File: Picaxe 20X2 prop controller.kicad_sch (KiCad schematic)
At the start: 58 parts, among them J1 FC68131, J10 Conn_01x05_Male (- power bus), J11 Conn_01x08_Male - pin I/O, J12 MP3 player, J13 servo 2, J14 servo 3, J15 servo 4, J16 servo 5, J17 Ext servo power, J18 Servo power select, J19 C.0, J2 Conn_01x08_Male - pin I/O, J20 C.5, J21 C.1, J22 C.6, J23 C.2, J24 C.7, J25 C.3, J26 C.4, J27 B.6 TX, J28 OSTTC080162, J29 B.7 RX, J3 servo 1, J4 servo 6, J5 B.7 RX, J6 OSTTC080162, J7 OSTTC020162, J8 PJ-202AH, J9 Conn_01x05_Male (+ power bus), U1 Picaxe 20X2, U3 L7805CV, U4 ULN2803A

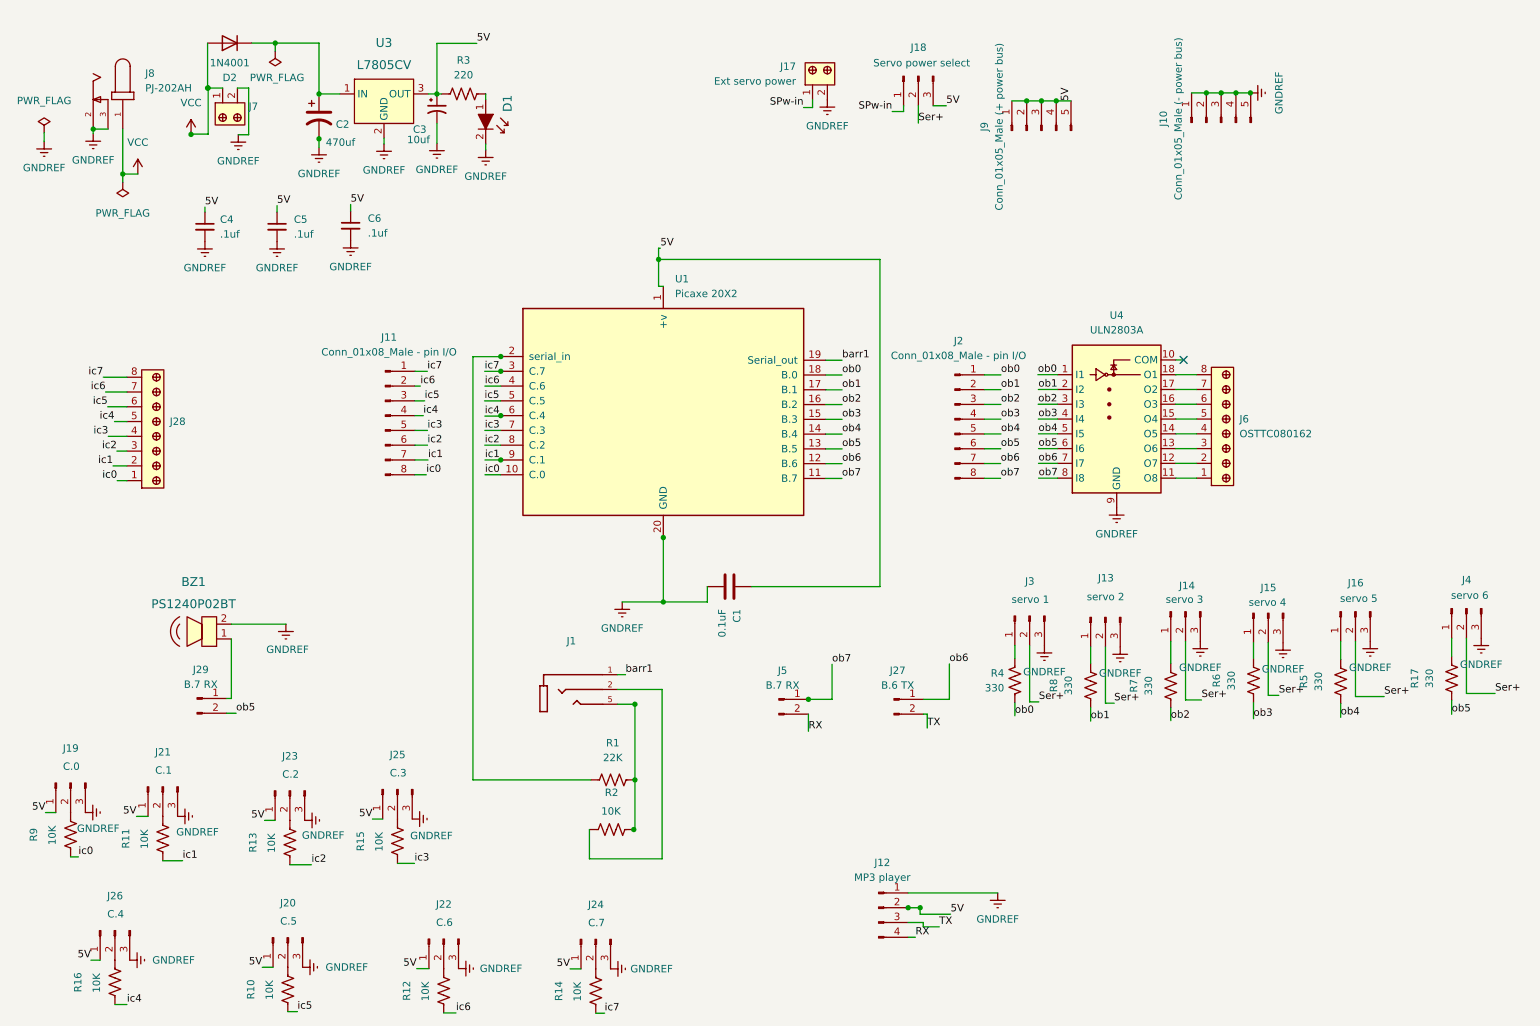
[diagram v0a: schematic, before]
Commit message: Move 20X2 to Git
Will branch to see about moving the I2C connector
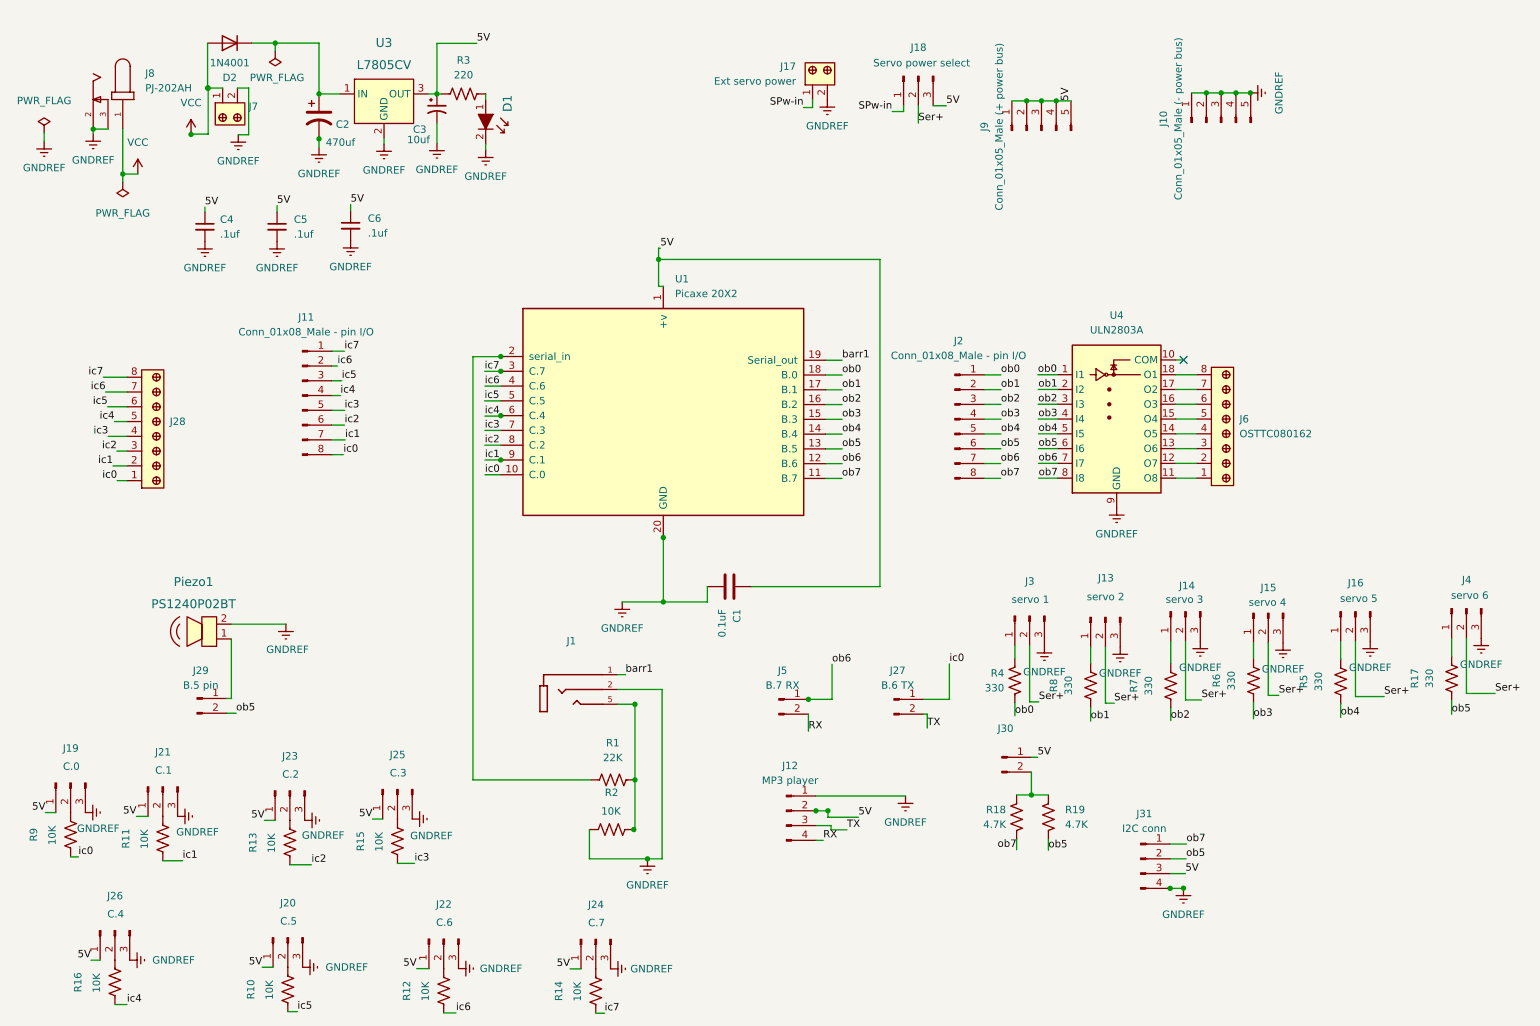
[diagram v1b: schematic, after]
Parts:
- added J30: B.6, Connector_PinHeader_2.54mm:PinHeader_1x02_P2.54mm_Vertical, symbol Connector:Conn_01x02_Male
- added J31: I2C conn, Connector_PinHeader_2.54mm:PinHeader_1x04_P2.54mm_Vertical, symbol Connector:Conn_01x04_Male
- added R18, R19: 4.7K, Resistor_THT:R_Axial_DIN0207_L6.3mm_D2.5mm_P10.16mm_Horizontal, symbol Device:R_US
- J29: value B.7 RX -> B.5 pin
- renumbered BZ1 to Piezo1
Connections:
- net 5V: now also J30.1 (Pin_1), J31.3 (Pin_3)
- net GNDREF: now also J1.2, R2.2, J31.4 (Pin_4)
- net ic0: now also J27.1 (Pin_1)
- net ob5: now also J31.2 (Pin_2), R19.2
- net ob6: now also J5.1 (Pin_1); no longer J27.1 (Pin_1)
- net ob7: now also J31.1 (Pin_1), R18.1; no longer J5.1 (Pin_1)
- new net: J30.2 (Pin_2), R18.2, R19.1
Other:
- moved on the sheet: J11, J12

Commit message: Moved I2C connector and started to add a battery select
Created a branch to move the I2C connector
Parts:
- added J32: B.6, Connector_PinHeader_2.54mm:PinHeader_1x02_P2.54mm_Vertical, symbol Connector:Conn_01x02_Male
- added J?: Batt / Reg select, Connector_PinHeader_2.54mm:PinHeader_1x03_P2.54mm_Vertical, symbol Connector:Conn_01x03_Male
- added J?: Batt Connector, Connector_PinHeader_2.54mm:PinHeader_1x02_P2.54mm_Vertical, symbol Connector:Conn_01x02_Male
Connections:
- net 5V: now also R18.2, R19.1; no longer J30.1 (Pin_1)
- net ob5: now also J32.1 (Pin_1); no longer J31.2 (Pin_2), R19.2
- net ob7: now also J30.1 (Pin_1); no longer J31.1 (Pin_1), R18.1
- new net I2CP1: J30.2 (Pin_2), J31.1 (Pin_1), R18.1
- new net I2CP2: J31.2 (Pin_2), J32.2 (Pin_2), R19.2
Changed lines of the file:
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@@
   (junction (at 216.535 22.6314) (diameter 0) (color 0 0 0 0)
   )
-  (junction (at 186.4614 143.3068) (diameter 0) (color 0 0 0 0)
-  )
   (junction (at 95.25 78.105) (diameter 0) (color 0 0 0 0)
   )
@@
   (junction (at 221.615 22.6314) (diameter 0) (color 0 0 0 0)
   )
+  (junction (at 183.9214 142.875) (diameter 0) (color 0 0 0 0)
+  )
   (junction (at 44.958 21.7932) (diameter 0) (color 0 0 0 0)
   )
@@
   )
   (junction (at 148.1328 126.873) (diameter 0) (color 0 0 0 0)
+  )
+  (junction (at 186.4614 139.3698) (diameter 0) (color 0 0 0 0)
   )
   (junction (at 123.19 110.1344) (diameter 0) (color 0 0 0 0)
@@
     (stroke (width 0) (type default) (color 0 0 0 0))
   )
+  (wire (pts (xy 183.9214 142.875) (xy 183.9214 143.3068))
+    (stroke (width 0) (type default) (color 0 0 0 0))
+  )
   (wire (pts (xy 24.8158 171.704) (xy 26.3906 171.704))
     (stroke (width 0) (type default) (color 0 0 0 0))
@@
     (stroke (width 0) (type default) (color 0 0 0 0))
   )
+  (wire (pts (xy 182.245 142.875) (xy 183.9214 142.875))
+    (stroke (width 0) (type default) (color 0 0 0 0))
+  )
   (wire (pts (xy 95.25 70.485) (xy 95.2754 70.485))
     (stroke (width 0) (type default) (color 0 0 0 0))
@@
     (stroke (width 0) (type default) (color 0 0 0 0))
   )
-  (wire (pts (xy 183.9214 143.3068) (xy 186.4614 143.3068))
-    (stroke (width 0) (type default) (color 0 0 0 0))
-  )
   (wire (pts (xy 187.579 71.0692) (xy 190.9572 71.0692))
     (stroke (width 0) (type default) (color 0 0 0 0))
@@
     (stroke (width 0) (type default) (color 0 0 0 0))
   )
-  (wire (pts (xy 186.4614 139.3698) (xy 186.4614 143.3068))
-    (stroke (width 0) (type default) (color 0 0 0 0))
-  )
   (wire (pts (xy 92.5068 73.025) (xy 95.25 73.025))
     (stroke (width 0) (type default) (color 0 0 0 0))
@@
     (stroke (width 0) (type default) (color 0 0 0 0))
   )
+  (wire (pts (xy 186.436 139.3698) (xy 186.4614 139.3698))
+    (stroke (width 0) (type default) (color 0 0 0 0))
+  )
   (wire (pts (xy 261.239 125.857) (xy 266.1666 125.857))
     (stroke (width 0) (type default) (color 0 0 0 0))
@@
     (stroke (width 0) (type default) (color 0 0 0 0))
   )
+  (wire (pts (xy 202.184 136.8552) (xy 203.4032 136.8552))
+    (stroke (width 0) (type default) (color 0 0 0 0))
+  )
   (wire (pts (xy 151.13 81.28) (xy 153.924 81.28))
     (stroke (width 0) (type default) (color 0 0 0 0))
@@
     (stroke (width 0) (type default) (color 0 0 0 0))
   )
+  (wire (pts (xy 186.4614 139.3698) (xy 187.7568 139.3698))
+    (stroke (width 0) (type default) (color 0 0 0 0))
+  )
   (wire (pts (xy 164.4904 25.8318) (xy 162.5346 25.8318))
     (stroke (width 0) (type default) (color 0 0 0 0))
@@
     (stroke (width 0) (type default) (color 0 0 0 0))
   )
+  (wire (pts (xy 202.184 139.3952) (xy 203.7842 139.3952))
+    (stroke (width 0) (type default) (color 0 0 0 0))
+  )
   (wire (pts (xy 211.2772 88.8492) (xy 214.8586 88.8492))
     (stroke (width 0) (type default) (color 0 0 0 0))
@@
     (stroke (width 0) (type default) (color 0 0 0 0))
   )
+  (wire (pts (xy 189.3824 142.875) (xy 183.9214 142.875))
+    (stroke (width 0) (type default) (color 0 0 0 0))
+  )
   (wire (pts (xy 187.706 88.8492) (xy 190.9572 88.8492))
     (stroke (width 0) (type default) (color 0 0 0 0))
@@
     (stroke (width 0) (type default) (color 0 0 0 0))
   )
-  (wire (pts (xy 186.4614 143.3068) (xy 189.3824 143.3068))
-    (stroke (width 0) (type default) (color 0 0 0 0))
-  )
   (wire (pts (xy 178.3842 78.7146) (xy 181.229 78.7146))
     (stroke (width 0) (type default) (color 0 0 0 0))
@@
     (stroke (width 0) (type default) (color 0 0 0 0))
   )
+  (wire (pts (xy 189.3824 143.3068) (xy 189.3824 142.875))
+    (stroke (width 0) (type default) (color 0 0 0 0))
+  )
   (wire (pts (xy 122.3772 51.2572) (xy 122.3772 49.3268))
     (stroke (width 0) (type default) (color 0 0 0 0))
@@
     (effects (font (size 1.27 1.27)) (justify left bottom))
   )
+  (label "I2CP1" (at 183.9214 152.7302 180)
+    (effects (font (size 1.27 1.27)) (justify right bottom))
+  )
   (label "5V" (at 122.682 49.3268 0)
+    (effects (font (size 1.27 1.27)) (justify left bottom))
+  )
+  (label "I2CP2" (at 203.7842 139.3952 0)
     (effects (font (size 1.27 1.27)) (justify left bottom))
   )
@@
     (effects (font (size 1.27 1.27)) (justify left bottom))
   )
+  (label "I2CP1" (at 187.7568 139.3698 0)
+    (effects (font (size 1.27 1.27)) (justify left bottom))
+  )
   (label "ic1" (at 68.5038 82.2706 0)
     (effects (font (size 1.27 1.27)) (justify left bottom))
@@
     (effects (font (size 1.27 1.27)) (justify left bottom))
   )
+  (label "BR_Sel" (at 30.607 50.419 0)
+    (effects (font (size 1.27 1.27)) (justify left bottom))
+  )
   (label "ob5" (at 187.6806 83.7692 0)
     (effects (font (size 1.27 1.27)) (justify left bottom))
@@
   )
   (label "barr1" (at 153.924 68.58 0)
-    (effects (font (size 1.27 1.27)) (justify left bottom))
-  )
-  (label "ob7" (at 213.106 151.7396 0)
     (effects (font (size 1.27 1.27)) (justify left bottom))
   )
@@
     (effects (font (size 1.27 1.27)) (justify left bottom))
   )
-  (label "ob5" (at 213.0552 154.2796 0)
-    (effects (font (size 1.27 1.27)) (justify left bottom))
-  )
   (label "Ser+" (at 187.7314 127.3048 0)
     (effects (font (size 1.27 1.27)) (justify left bottom))
@@
     (effects (font (size 1.27 1.27)) (justify left bottom))
   )
+  (label "I2CP1" (at 213.106 151.7396 0)
+    (effects (font (size 1.27 1.27)) (justify left bottom))
+  )
   (label "ic4" (at 92.5068 78.1812 0)
     (effects (font (size 1.27 1.27)) (justify left bottom))
@@
     (effects (font (size 1.27 1.27)) (justify left bottom))
   )
-  (label "ob7" (at 183.9214 152.7302 180)
-    (effects (font (size 1.27 1.27)) (justify right bottom))
+  (label "ob7" (at 187.5282 136.8298 0)
+    (effects (font (size 1.27 1.27)) (justify left bottom))
   )
   (label "ob7" (at 181.1782 88.8746 0)
@@
     (effects (font (size 1.27 1.27)) (justify left bottom))
   )
-  (label "5V" (at 187.5282 136.8298 0)
-    (effects (font (size 1.27 1.27)) (justify left bottom))
+  (label "5V" (at 182.245 142.875 180)
+    (effects (font (size 1.27 1.27)) (justify right bottom))
   )
   (label "5V" (at 54.6608 147.6756 180)
@@
     (effects (font (size 1.27 1.27)) (justify right bottom))
   )
-  (label "ob5" (at 189.3824 152.8064 0)
+  (label "ob5" (at 203.4032 136.8552 0)
     (effects (font (size 1.27 1.27)) (justify left bottom))
   )
@@
     (effects (font (size 1.27 1.27)) (justify right bottom))
   )
+  (label "I2CP2" (at 213.0552 154.2796 0)
+    (effects (font (size 1.27 1.27)) (justify left bottom))
+  )
   (label "TX" (at 154.7622 149.3012 0)
     (effects (font (size 1.27 1.27)) (justify left bottom))
@@
   )
   (label "ob3" (at 181.229 78.7146 0)
+    (effects (font (size 1.27 1.27)) (justify left bottom))
+  )
+  (label "I2CP2" (at 189.3824 152.8064 0)
     (effects (font (size 1.27 1.27)) (justify left bottom))
   )
@@
     )
     (pin "1")
+  )
+  (symbol (lib_id "Connector:Conn_01x02_Male") (at 197.104 136.8552 0) (unit 1)
+    (in_bom yes) (on_board yes) (fields_autoplaced)
+    (property "Reference" "J32" (id 0) (at 197.739 131.9022 0))
+    (property "Value" "B.6" (id 1) (at 197.739 134.4422 0)
+      (effects (font (size 1.27 1.27)) hide)
+    )
+    (property "Footprint" "Connector_PinHeader_2.54mm:PinHeader_1x02_P2.54mm_Vertical" (id 2) (at 197.104 136.8552 0)
+      (effects (font (size 1.27 1.27)) hide)
+    )
+    (property "Datasheet" "~" (id 3) (at 197.104 136.8552 0)
+      (effects (font (size 1.27 1.27)) hide)
+    )
+    (pin "1")
+    (pin "2")
   )
   (symbol (lib_id "Picaxe_Joe:LTL2R3KEK") (at 92.6592 28.8544 270) (unit 1)
@@
     (pin "1")
   )
+  (symbol (lib_id "Connector:Conn_01x03_Male") (at 27.3304 62.0522 270) (mirror x) (unit 1)
+    (in_bom yes) (on_board yes)
+    (property "Reference" "J?" (id 0) (at 27.2923 66.9925 90))
+    (property "Value" "Batt / Reg select" (id 1) (at 26.7589 64.3255 90))
+    (property "Footprint" "Connector_PinHeader_2.54mm:PinHeader_1x03_P2.54mm_Vertical" (id 2) (at 27.3304 62.0522 0)
+      (effects (font (size 1.27 1.27)) hide)
+    )
+    (property "Datasheet" "~" (id 3) (at 27.3304 62.0522 0)
+      (effects (font (size 1.27 1.27)) hide)
+    )
+    (pin "1")
+    (pin "2")
+    (pin "3")
+  )
   (symbol (lib_id "Connector:Conn_01x04_Male") (at 144.3482 146.0246 0) (unit 1)
     (in_bom yes) (on_board yes) (fields_autoplaced)
@@
     (pin "1")
   )
+  (symbol (lib_id "Connector:Conn_01x02_Male") (at 20.066 50.2158 0) (unit 1)
+    (in_bom yes) (on_board yes) (fields_autoplaced)
+    (property "Reference" "J?" (id 0) (at 20.701 45.2628 0))
+    (property "Value" "Batt Connector" (id 1) (at 20.701 47.8028 0))
+    (property "Footprint" "Connector_PinHeader_2.54mm:PinHeader_1x02_P2.54mm_Vertical" (id 2) (at 20.066 50.2158 0)
+      (effects (font (size 1.27 1.27)) hide)
+    )
+    (property "Datasheet" "~" (id 3) (at 20.066 50.2158 0)
+      (effects (font (size 1.27 1.27)) hide)
+    )
+    (pin "1")
+    (pin "2")
+  )
   (symbol (lib_id "Connector:Conn_01x03_Male") (at 199.1868 112.776 90) (mirror x) (unit 1)
     (in_bom yes) (on_board yes)
@@
       (reference "J31") (unit 1) (value "I2C conn") (footprint "Connector_PinHeader_2.54mm:PinHeader_1x04_P2.54mm_Vertical")
     )
+    (path "/0bafae2e-441b-4483-84b4-f9087ac28dea"
+      (reference "J32") (unit 1) (value "B.6") (footprint "Connector_PinHeader_2.54mm:PinHeader_1x02_P2.54mm_Vertical")
+    )
+    (path "/571822e8-0e38-4fc2-9bfc-81299bd0b279"
+      (reference "J?") (unit 1) (value "Batt / Reg select") (footprint "Connector_PinHeader_2.54mm:PinHeader_1x03_P2.54mm_Vertical")
+    )
+    (path "/8b60c28b-2164-4b2e-bb66-23cd9efd8df7"
+      (reference "J?") (unit 1) (value "Batt Connector") (footprint "Connector_PinHeader_2.54mm:PinHeader_1x02_P2.54mm_Vertical")
+    )
     (path "/cd32adbb-b86c-4eee-aa17-84272d12d149"

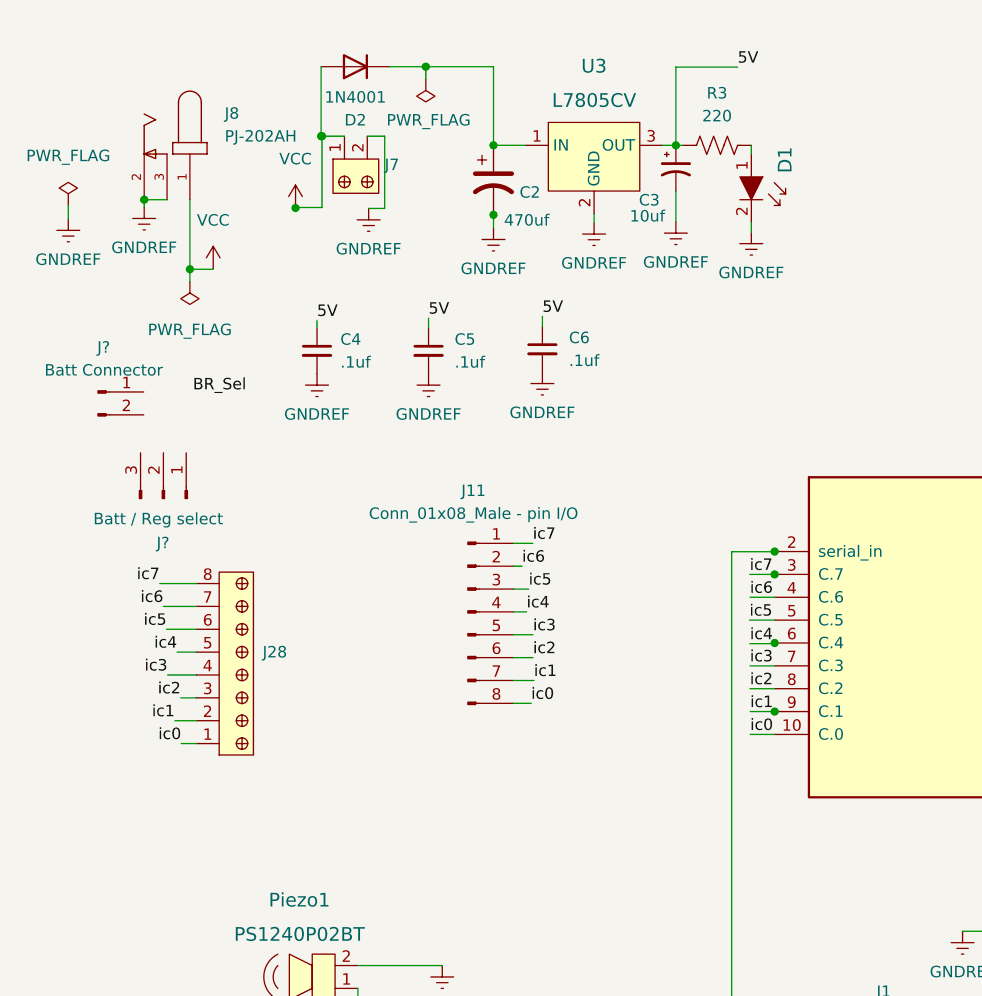
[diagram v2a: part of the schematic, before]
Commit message: Moved I2c connector and added battery select option
Added a battery connector and a select jumper to switch between the onboard regulator and the battery input connector. I also moved the I2C connector and added jumpers to disconnect the pins if needed.
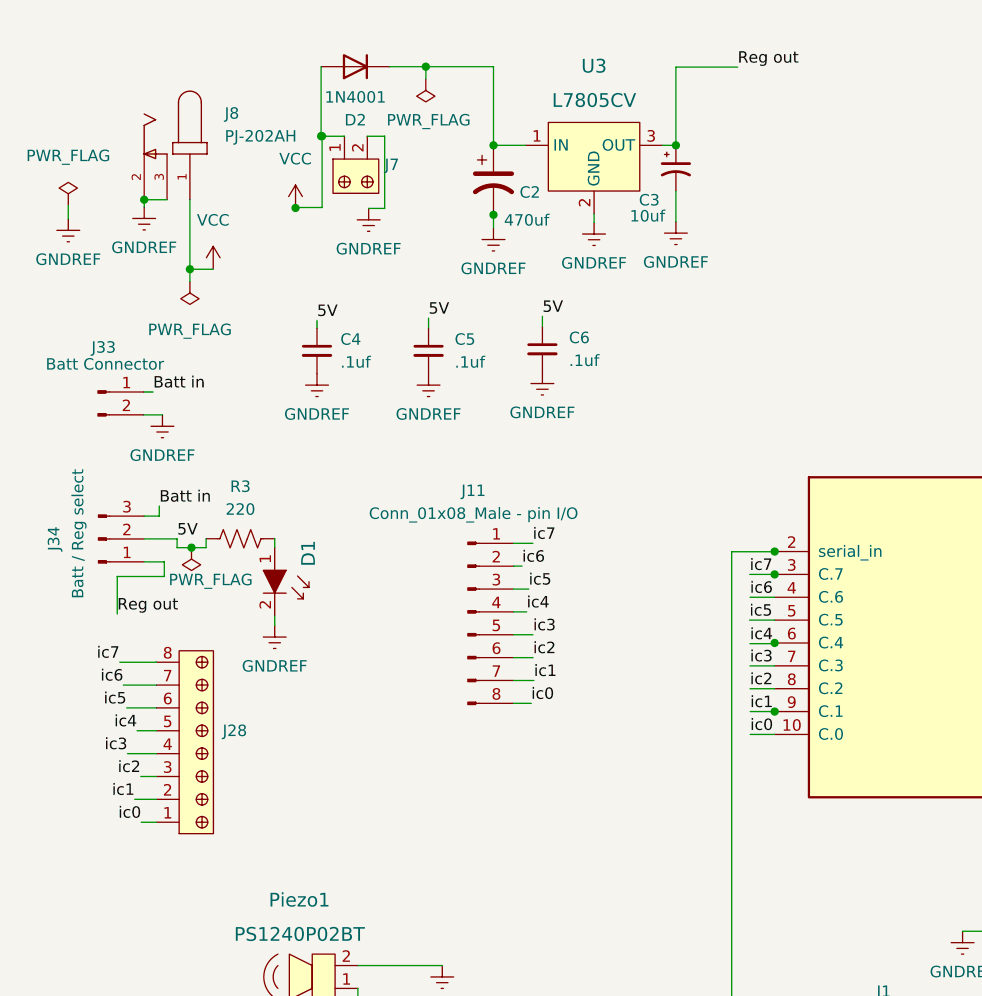
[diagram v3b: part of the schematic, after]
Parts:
- gave numbers to parts that had none: 2
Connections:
- net 5V: now also J34.2 (Pin_2); no longer C3.1, U3.3 (OUT)
- net GNDREF: now also J33.2 (Pin_2)
- net Reg out: now reaches J34.1 (Pin_1)
- net Reg out: now also C3.1, U3.3 (OUT)
- net Batt in: now reaches J34.3 (Pin_3)
- net Batt in: now also J33.1 (Pin_1)
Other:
- moved on the sheet: D1, J28, J34, R3
